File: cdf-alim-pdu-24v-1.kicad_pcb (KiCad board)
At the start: 2 copper layers, 80 x 60 mm, 130 parts, among them J1 Conn_01x02, J10 Conn_01x02, J11 Conn_01x02, J12 Conn_01x02, J13 Conn_01x02, J14 Conn_01x02, J15 Conn_01x02, J16 Conn_01x02, J17 Conn_01x02, J2 Conn_01x02, J3 Conn_01x02, J4 Conn_01x02, J5 Conn_01x02, J6 Conn_01x02, J7 Conn_01x02, J8 Conn_01x02, J9 Conn_01x02, Q1 BSC019N04LS, Q2 BSC019N04LS, Q3 BSC019N04LS, U1 TPS25983, U2 TPS25983, U3 TPS25983, U4 HT753-1, U5 MX25947, U6 MX25947, U7 MX25947

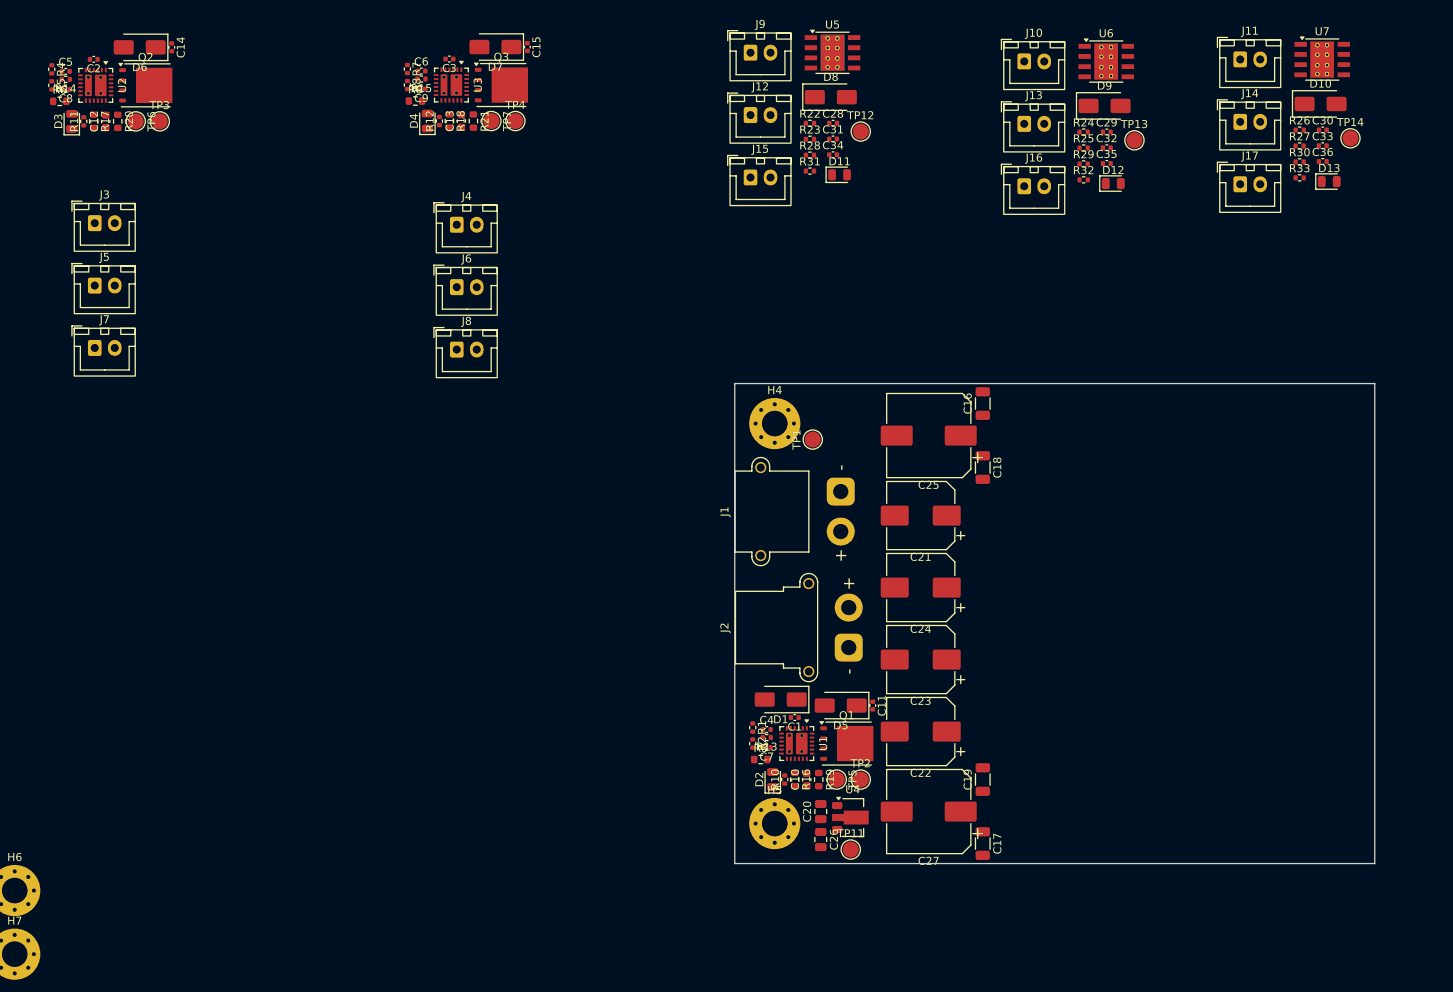
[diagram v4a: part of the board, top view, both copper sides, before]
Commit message: pcb: route high I efuses
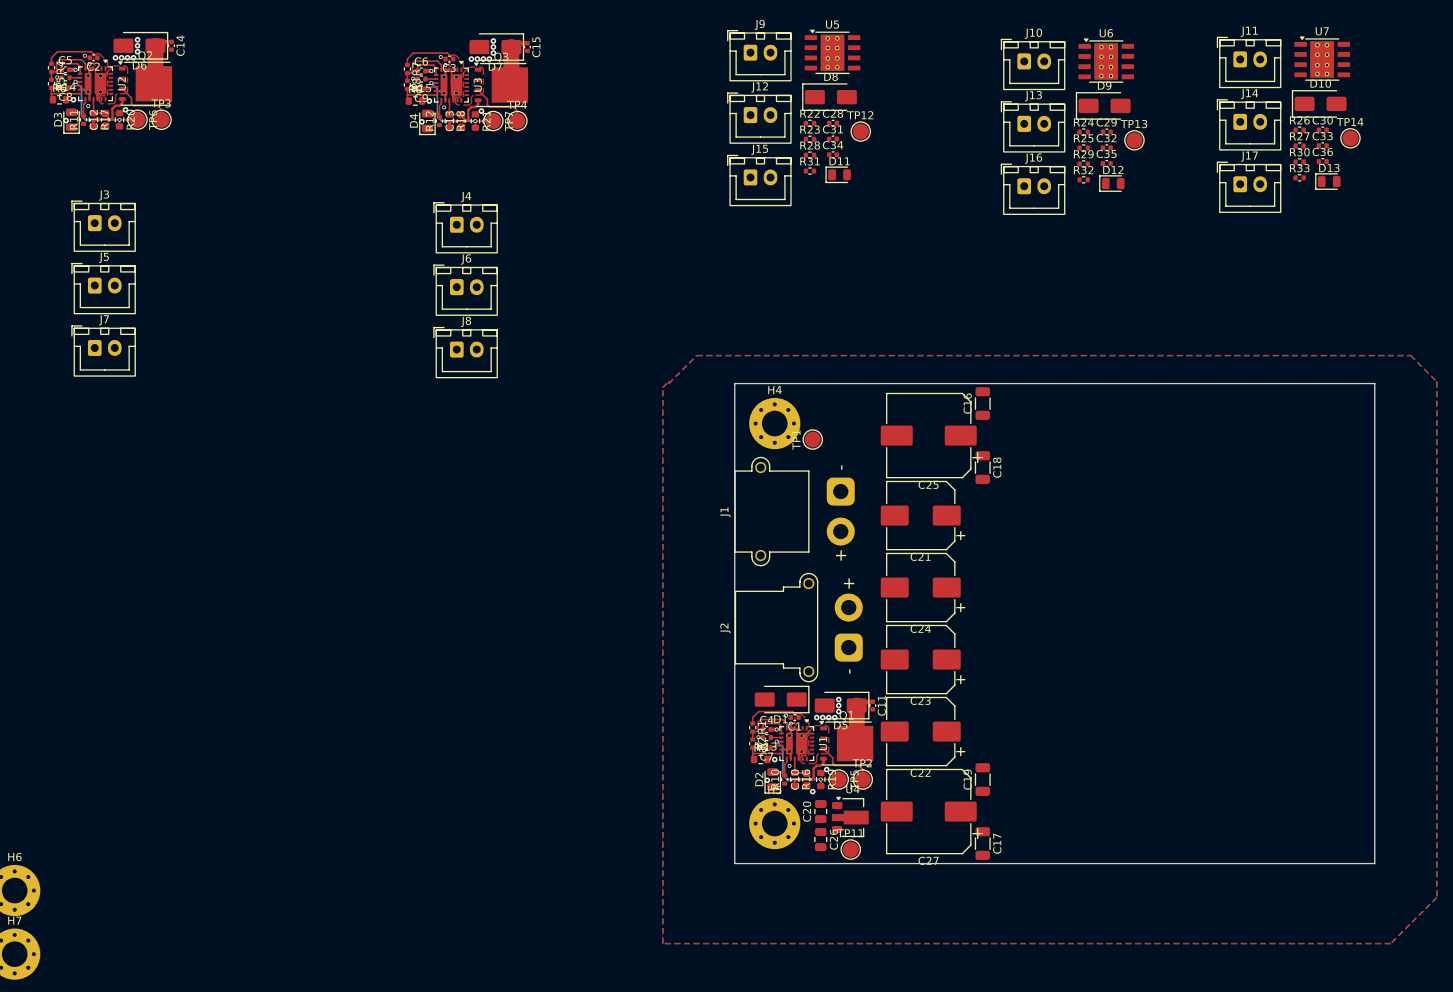
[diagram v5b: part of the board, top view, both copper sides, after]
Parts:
- moved R20 0.30 mm to (83.1, 47.0)
- moved TP3 0.30 mm to (88.3, 47.0)
- moved TP6 0.30 mm to (85.3, 47.0)
- moved R19 0.25 mm to (170.8, 129.5)
- moved R21 0.25 mm to (127.6, 47.2)
- moved TP2 0.25 mm to (176.0, 129.5)
- moved TP4 0.25 mm to (132.8, 47.2)
- moved TP5 0.25 mm to (173.0, 129.5)
- moved TP7 0.25 mm to (129.8, 47.2)
- moved C12 0.20 mm to (81.3, 47.0)
- moved C14 0.20 mm to (89.6, 37.8)
- moved C2 0.20 mm to (79.8, 39.3)
- moved C5 0.20 mm to (76.3, 40.8)
- moved C8 0.20 mm to (76.3, 43.0)
- moved D3 0.20 mm to (77.1, 47.0)
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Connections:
- C1 pad 1: Net-(C1-Pad1) -> +24V_IN
- C2 pad 1: Net-(C2-Pad1) -> +24V
- C3 pad 1: Net-(C3-Pad1) -> +24V
- D1 pad 1: Net-(D1-A1) -> +24V_IN
- J1 pad 2: Net-(D1-A1) -> +24V_IN
- J2 pad 2: Net-(D1-A1) -> +24V_IN
- R1 pad 1: Net-(C1-Pad1) -> +24V_IN
- R4 pad 1: Net-(C2-Pad1) -> +24V
- R7 pad 1: Net-(C3-Pad1) -> +24V
- TP1 pad 1: Net-(D1-A1) -> +24V_IN
- U1 pad 1: Net-(C1-Pad1) -> +24V_IN
- U1 pad 16: Net-(C1-Pad1) -> +24V_IN
- U1 pad 2: Net-(C1-Pad1) -> +24V_IN
- U1 pad 25: Net-(C1-Pad1) -> +24V_IN
- U1 pad 3: Net-(C1-Pad1) -> +24V_IN
- U2 pad 1: Net-(C2-Pad1) -> +24V
- U2 pad 16: Net-(C2-Pad1) -> +24V
- U2 pad 2: Net-(C2-Pad1) -> +24V
- U2 pad 25: Net-(C2-Pad1) -> +24V
- U2 pad 3: Net-(C2-Pad1) -> +24V
- U3 pad 1: Net-(C3-Pad1) -> +24V
- U3 pad 16: Net-(C3-Pad1) -> +24V
- U3 pad 2: Net-(C3-Pad1) -> +24V
- U3 pad 25: Net-(C3-Pad1) -> +24V
- U3 pad 3: Net-(C3-Pad1) -> +24V
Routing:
- net +24V: track 0.00 -> 23.4 mm
- net Net-(U3-IMON): track 0.00 -> 13.2 mm, vias 0 -> 2
- net Net-(U2-IMON): track 0.00 -> 13.2 mm, vias 0 -> 2
- net Net-(U1-IMON): track 0.00 -> 13.2 mm, vias 0 -> 2
- net GND: track 0.00 -> 12.8 mm, vias 0 -> 49
- net +24V_IN: track 0.00 -> 8.17 mm
- net Net-(Q3-S-Pad1): track 0.00 -> 7.65 mm
- net Net-(Q2-S-Pad1): track 0.00 -> 7.65 mm
- net Net-(Q1-S-Pad1): track 0.00 -> 7.65 mm
- net Net-(U2-EN/UVLO): track 0.00 -> 7.24 mm
- net Net-(U1-EN/UVLO): track 0.00 -> 7.24 mm
- net Net-(U3-EN/UVLO): track 0.00 -> 7.24 mm
- net Net-(D7-K): track 0.00 -> 7.03 mm
- net Net-(D6-K): track 0.00 -> 7.03 mm
- net Net-(Q3-G): track 0.00 -> 6.31 mm
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- added copper zone on F.Cu, net +24V
- added copper zone on F.Cu, net +24V_IN
- added copper zone on B.Cu, net GND
- added copper zone on F.Cu, net GND
- added copper zone on F.Cu, net Net-(Q1-S-Pad1)
- added copper zone on F.Cu, net Net-(Q2-S-Pad1)
- added copper zone on F.Cu, net Net-(Q3-S-Pad1)

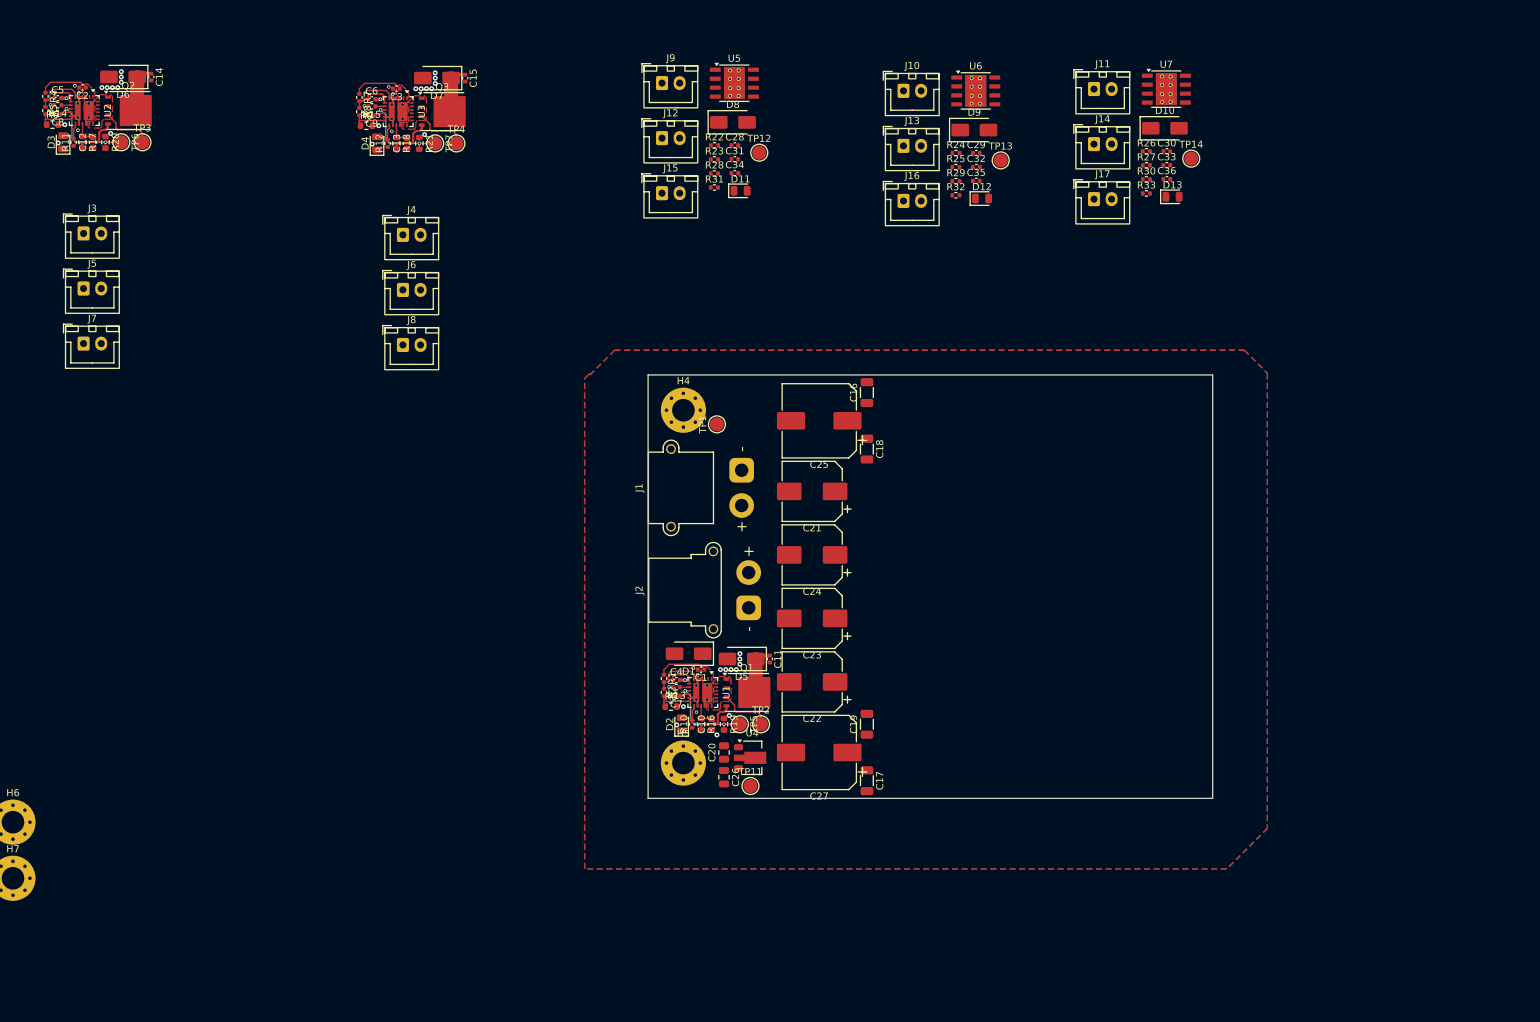
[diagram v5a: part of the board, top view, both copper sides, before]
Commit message: pcb: add high I efuses placement
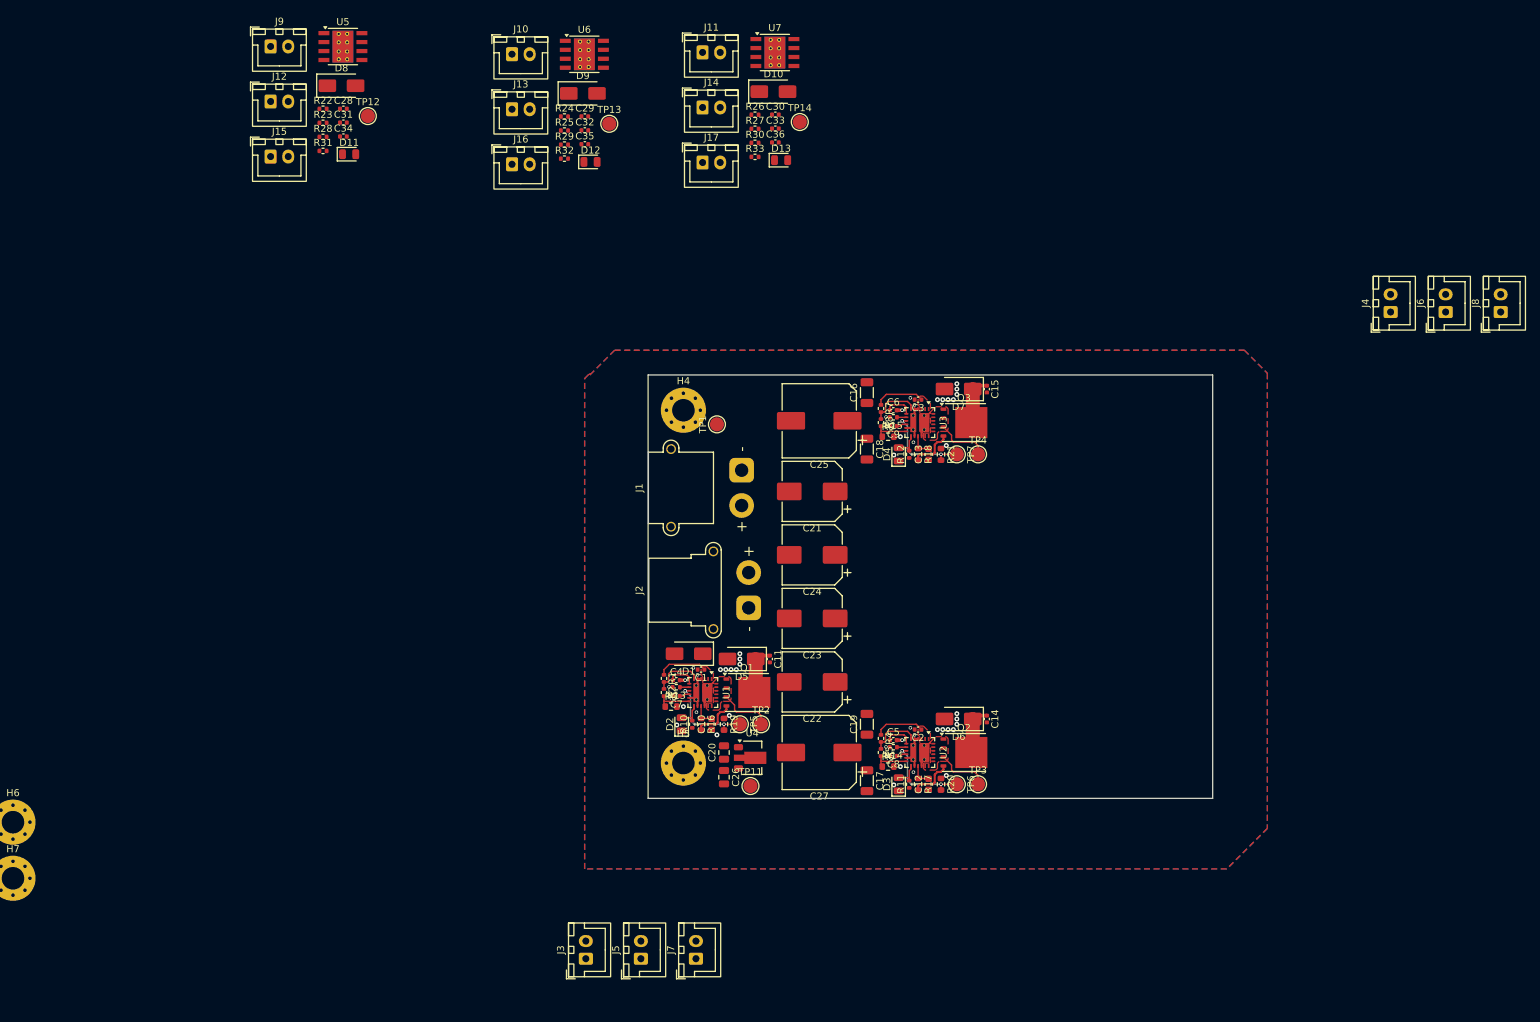
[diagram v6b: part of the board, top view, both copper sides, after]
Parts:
- moved J8 155.6 mm to (280.8, 71.1), turned to 90 degrees
- moved C12 149.3 mm to (199.8, 138.0)
- moved C14 149.3 mm to (208.0, 128.8)
- moved C2 149.3 mm to (198.2, 130.2)
- moved C5 149.3 mm to (194.8, 131.8)
- moved C8 149.3 mm to (194.8, 134.0)
- moved D3 149.3 mm to (195.5, 138.0)
- moved D6 149.3 mm to (204.0, 128.8)
- moved Q2 149.3 mm to (204.8, 133.5)
- moved R11 149.3 mm to (197.0, 138.0)
- moved R14 149.3 mm to (194.8, 132.8)
- moved R17 149.3 mm to (198.2, 138.0)
- moved R20 149.3 mm to (201.5, 138.0)
- moved R4 149.3 mm to (193.0, 131.5)
- moved R5 149.3 mm to (193.0, 133.5)
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
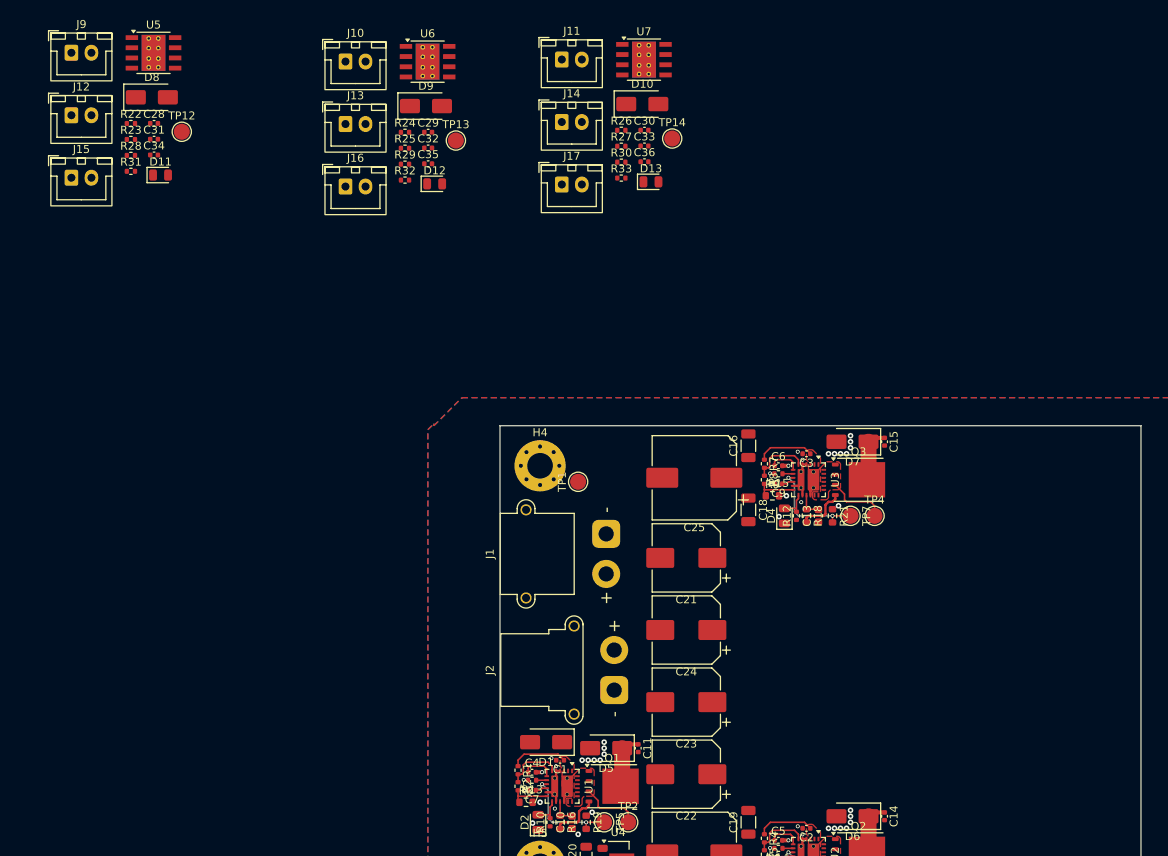
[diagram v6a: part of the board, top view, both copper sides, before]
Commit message: pcb: add low I efuses placement/layout
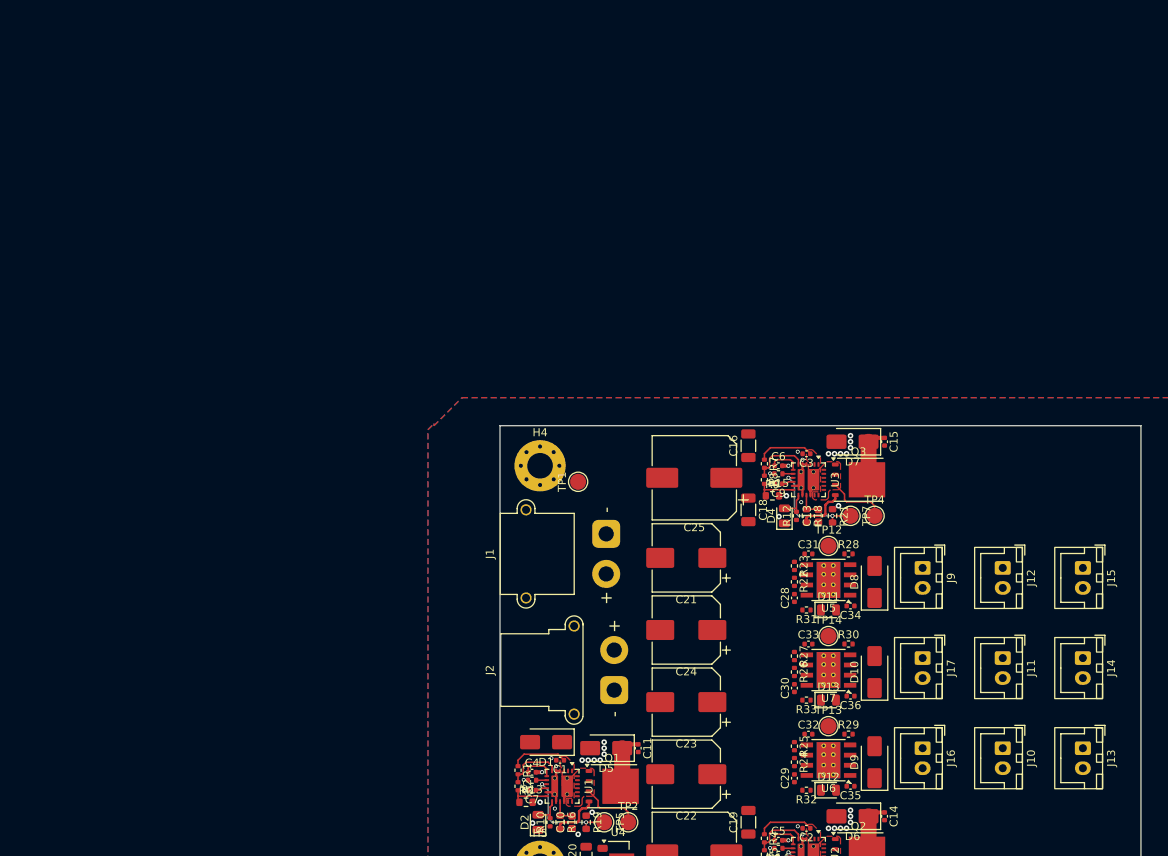
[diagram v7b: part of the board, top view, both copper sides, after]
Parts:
- moved J15 135.3 mm to (232.8, 97.8), turned to -90 degrees
- moved J12 129.3 mm to (222.8, 97.8), turned to -90 degrees
- moved J9 124.2 mm to (212.8, 97.8), turned to -90 degrees
- moved J13 120.6 mm to (232.8, 120.2), turned to -90 degrees
- moved J10 118.6 mm to (222.8, 120.2), turned to -90 degrees
- moved D8 108.6 mm to (206.8, 99.5), turned to 90 degrees
- moved U5 106.9 mm to (201.0, 99.2), turned to 180 degrees
- moved C34 103.6 mm to (203.8, 102.5), turned to 180 degrees
- moved R28 102.5 mm to (203.5, 96.0)
- moved R22 100.7 mm to (196.8, 99.5), turned to -90 degrees
- moved R31 100.5 mm to (198.2, 103.0), turned to 180 degrees
- moved U6 100.5 mm to (201.0, 121.8), turned to 180 degrees
- moved J16 100.5 mm to (212.8, 120.2), turned to -90 degrees
- moved D11 99.5 mm to (201.0, 103.0)
- moved C28 99.5 mm to (196.8, 101.5), turned to 90 degrees
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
